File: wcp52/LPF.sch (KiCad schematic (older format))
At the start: 13 parts

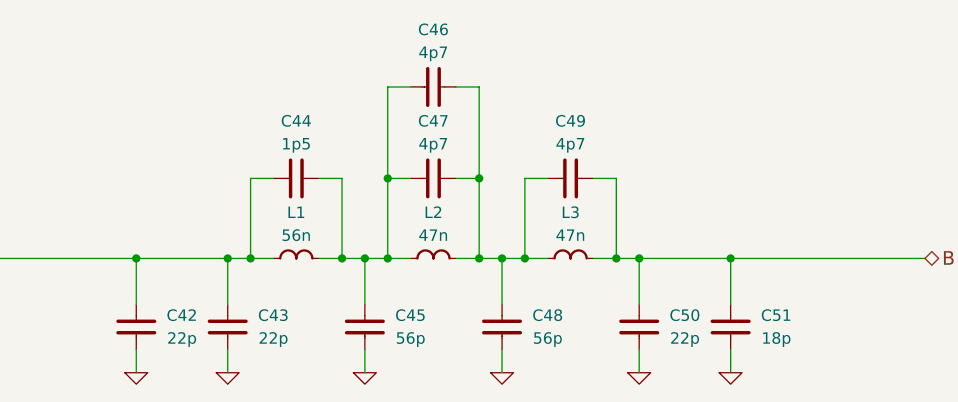
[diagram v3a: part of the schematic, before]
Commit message: Reannotate parts. May need to tweak silkscreen
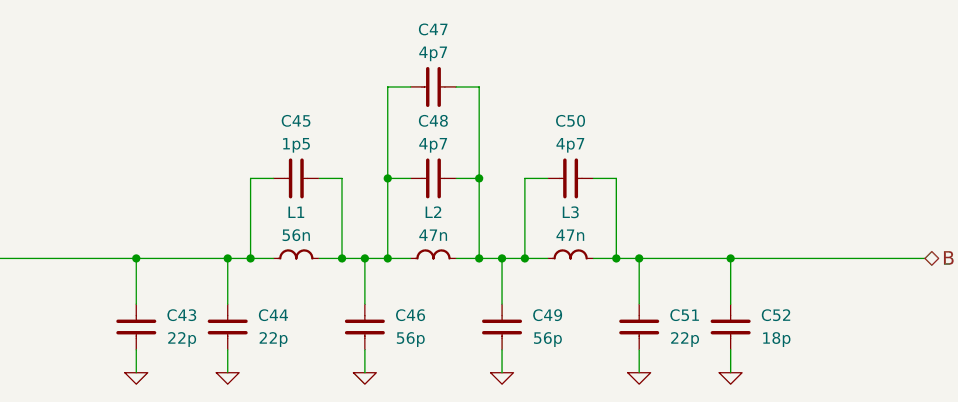
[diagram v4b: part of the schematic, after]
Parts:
- C43: renamed from C42; OldReference (none) -> C42
- C44: renamed from C43; OldReference (none) -> C43
- C45: renamed from C44; OldReference (none) -> C44
- C46: renamed from C45; OldReference (none) -> C45
- C47: renamed from C46; OldReference (none) -> C46
- C48: renamed from C47; OldReference (none) -> C47
- C49: renamed from C48; OldReference (none) -> C48
- C50: renamed from C49; OldReference (none) -> C49
- C51: renamed from C50; OldReference (none) -> C50
- C52: renamed from C51; OldReference (none) -> C51
- L1: OldReference (none) -> L1
- L2: OldReference (none) -> L2
- L3: OldReference (none) -> L3
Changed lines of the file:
@@
 B
 $Comp
-L C-0402 C42
+L C-0402 C43
 U 1 1 54F2BD52
 P 5550 3700
-F 0 "C42" H 5750 3750 50  0000 C CNN
+F 0 "C43" H 5750 3750 50  0000 C CNN
 F 1 "22p" H 5750 3650 50  0000 C CNN
 F 2 "IPC7351-Nominal:CAPC1005X55" H 5550 3700 50  0001 C CNN
@@
 F 5 "Murata" H 5550 3700 60  0001 C CNN "Manuf"
 F 6 "DIST DIGIKEY 490-6219-1-ND" H 6350 4250 60  0001 C CNN "BOM"
+F 7 "C42" H 5550 3700 50  0001 C CNN "OldReference"
 	1    5550 3700
 	1    0    0    -1
@@
 F 5 "Samsung" H 6250 3400 60  0001 C CNN "Manuf"
 F 6 "DIST DIGIKEY 1276-6281-1-ND" H 6250 3400 60  0001 C CNN "BOM"
+F 7 "L1" H 6250 3400 50  0001 C CNN "OldReference"
 	1    6250 3400
 	0    1    1    0
 $EndComp
 $Comp
-L C-0402 C43
+L C-0402 C44
 U 1 1 54F2C0F9
 P 5950 3700
-F 0 "C43" H 6150 3750 50  0000 C CNN
+F 0 "C44" H 6150 3750 50  0000 C CNN
 F 1 "22p" H 6150 3650 50  0000 C CNN
 F 2 "IPC7351-Nominal:CAPC1005X55" H 5950 3700 50  0001 C CNN
@@
 F 5 "Murata" H 5950 3700 60  0001 C CNN "Manuf"
 F 6 "DIST DIGIKEY 490-6219-1-ND" H 6750 4250 60  0001 C CNN "BOM"
+F 7 "C43" H 5950 3700 50  0001 C CNN "OldReference"
 	1    5950 3700
 	1    0    0    -1
 $EndComp
 $Comp
-L C-0402 C44
+L C-0402 C45
 U 1 1 54F2C23D
 P 6250 3050
-F 0 "C44" V 6000 3050 50  0000 C CNN
+F 0 "C45" V 6000 3050 50  0000 C CNN
 F 1 "1p5" V 6100 3050 50  0000 C CNN
 F 2 "IPC7351-Nominal:CAPC1005X55" H 6250 3050 50  0001 C CNN
@@
 F 5 "Samsung" H 6250 3050 60  0001 C CNN "Manuf"
 F 6 "DIST DIGIKEY 1276-1071-1-ND" H 7050 3600 60  0001 C CNN "BOM"
+F 7 "C44" H 6250 3050 50  0001 C CNN "OldReference"
 	1    6250 3050
 	0    1    1    0
@@
 F 5 "Samsung" H 6850 3400 60  0001 C CNN "Manuf"
 F 6 "DIST DIGIKEY 1276-6280-1-ND" H 6850 3400 60  0001 C CNN "BOM"
+F 7 "L2" H 6850 3400 50  0001 C CNN "OldReference"
 	1    6850 3400
 	0    1    1    0
 $EndComp
 $Comp
-L C-0402 C47
+L C-0402 C48
 U 1 1 54F2CACC
 P 6850 3050
-F 0 "C47" V 6600 3050 50  0000 C CNN
+F 0 "C48" V 6600 3050 50  0000 C CNN
 F 1 "4p7" V 6700 3050 50  0000 C CNN
 F 2 "IPC7351-Nominal:CAPC1005X55" H 6850 3050 50  0001 C CNN
@@
 F 5 "Samsung" H 6850 3050 60  0001 C CNN "Manuf"
 F 6 "DIST DIGIKEY 1276-1703-1-ND" H 7650 3600 60  0001 C CNN "BOM"
+F 7 "C47" H 6850 3050 50  0001 C CNN "OldReference"
 	1    6850 3050
 	0    1    1    0
 $EndComp
 $Comp
-L C-0402 C46
+L C-0402 C47
 U 1 1 54F2CB7C
 P 6850 2650
-F 0 "C46" V 6600 2650 50  0000 C CNN
+F 0 "C47" V 6600 2650 50  0000 C CNN
 F 1 "4p7" V 6700 2650 50  0000 C CNN
 F 2 "IPC7351-Nominal:CAPC1005X55" H 6850 2650 50  0001 C CNN
@@
 F 5 "Samsung" H 6850 2650 60  0001 C CNN "Manuf"
 F 6 "DIST DIGIKEY 1276-1703-1-ND" H 7650 3200 60  0001 C CNN "BOM"
+F 7 "C46" H 6850 2650 50  0001 C CNN "OldReference"
 	1    6850 2650
 	0    1    1    0
@@
 F 5 "Samsung" H 7450 3400 60  0001 C CNN "Manuf"
 F 6 "DIST DIGIKEY 1276-6280-1-ND" H 7450 3400 60  0001 C CNN "BOM"
+F 7 "L3" H 7450 3400 50  0001 C CNN "OldReference"
 	1    7450 3400
 	0    1    1    0
 $EndComp
 $Comp
-L C-0402 C49
+L C-0402 C50
 U 1 1 54F2CBED
 P 7450 3050
-F 0 "C49" V 7200 3050 50  0000 C CNN
+F 0 "C50" V 7200 3050 50  0000 C CNN
 F 1 "4p7" V 7300 3050 50  0000 C CNN
 F 2 "IPC7351-Nominal:CAPC1005X55" H 7450 3050 50  0001 C CNN
@@
 F 5 "Samsung" H 7450 3050 60  0001 C CNN "Manuf"
 F 6 "DIST DIGIKEY 1276-1703-1-ND" H 8250 3600 60  0001 C CNN "BOM"
+F 7 "C49" H 7450 3050 50  0001 C CNN "OldReference"
 	1    7450 3050
 	0    1    1    0
 $EndComp
 $Comp
-L C-0402 C45
+L C-0402 C46
 U 1 1 54F2CE50
 P 6550 3700
-F 0 "C45" H 6750 3750 50  0000 C CNN
+F 0 "C46" H 6750 3750 50  0000 C CNN
 F 1 "56p" H 6750 3650 50  0000 C CNN
 F 2 "IPC7351-Nominal:CAPC1005X55" H 6550 3700 50  0001 C CNN
@@
 F 5 "Samsung" H 6550 3700 60  0001 C CNN "Manuf"
 F 6 "DIST DIGIKEY 1276-1707-1-ND" H 7350 4250 60  0001 C CNN "BOM"
+F 7 "C45" H 6550 3700 50  0001 C CNN "OldReference"
 	1    6550 3700
 	1    0    0    -1
 $EndComp
 $Comp
-L C-0402 C48
+L C-0402 C49
 U 1 1 54F2D3A4
 P 7150 3700
-F 0 "C48" H 7350 3750 50  0000 C CNN
+F 0 "C49" H 7350 3750 50  0000 C CNN
 F 1 "56p" H 7350 3650 50  0000 C CNN
 F 2 "IPC7351-Nominal:CAPC1005X55" H 7150 3700 50  0001 C CNN
@@
 F 5 "Samsung" H 7150 3700 60  0001 C CNN "Manuf"
 F 6 "DIST DIGIKEY 1276-1707-1-ND" H 7950 4250 60  0001 C CNN "BOM"
+F 7 "C48" H 7150 3700 50  0001 C CNN "OldReference"
 	1    7150 3700
 	1    0    0    -1
 $EndComp
 $Comp
-L C-0402 C50
+L C-0402 C51
 U 1 1 54F2D3DD
 P 7750 3700
-F 0 "C50" H 7950 3750 50  0000 C CNN
+F 0 "C51" H 7950 3750 50  0000 C CNN
 F 1 "22p" H 7950 3650 50  0000 C CNN
 F 2 "IPC7351-Nominal:CAPC1005X55" H 7750 3700 50  0001 C CNN
@@
 F 5 "Murata" H 7750 3700 60  0001 C CNN "Manuf"
 F 6 "DIST DIGIKEY 490-6219-1-ND" H 8550 4250 60  0001 C CNN "BOM"
+F 7 "C50" H 7750 3700 50  0001 C CNN "OldReference"
 	1    7750 3700
 	1    0    0    -1
 $EndComp
 $Comp
-L C-0402 C51
+L C-0402 C52
 U 1 1 54F2D417
 P 8150 3700
-F 0 "C51" H 8350 3750 50  0000 C CNN
+F 0 "C52" H 8350 3750 50  0000 C CNN
 F 1 "18p" H 8350 3650 50  0000 C CNN
 F 2 "IPC7351-Nominal:CAPC1005X55" H 8150 3700 50  0001 C CNN
@@
 F 5 "Samsung" H 8150 3700 60  0001 C CNN "Manuf"
 F 6 "DIST DIGIKEY 1276-1140-1-ND" H 8950 4250 60  0001 C CNN "BOM"
+F 7 "C51" H 8150 3700 50  0001 C CNN "OldReference"
 	1    8150 3700
 	1    0    0    -1
@@
 F 2 "" H 5550 3900 60  0000 C CNN
 F 3 "" H 5550 3900 60  0000 C CNN
+F 4 "#PWR0157" H 5550 3900 50  0001 C CNN "OldReference"
 	1    5550 3900
 	1    0    0    -1
@@
 F 2 "" H 5950 3900 60  0000 C CNN
 F 3 "" H 5950 3900 60  0000 C CNN
+F 4 "#PWR0158" H 5950 3900 50  0001 C CNN "OldReference"
 	1    5950 3900
 	1    0    0    -1
@@
 F 2 "" H 6550 3900 60  0000 C CNN
 F 3 "" H 6550 3900 60  0000 C CNN
+F 4 "#PWR0159" H 6550 3900 50  0001 C CNN "OldReference"
 	1    6550 3900
 	1    0    0    -1
@@
 F 2 "" H 7150 3900 60  0000 C CNN
 F 3 "" H 7150 3900 60  0000 C CNN
+F 4 "#PWR0160" H 7150 3900 50  0001 C CNN "OldReference"
 	1    7150 3900
 	1    0    0    -1
@@
 F 2 "" H 7750 3900 60  0000 C CNN
 F 3 "" H 7750 3900 60  0000 C CNN
+F 4 "#PWR0161" H 7750 3900 50  0001 C CNN "OldReference"
 	1    7750 3900
 	1    0    0    -1
@@
 F 2 "" H 8150 3900 60  0000 C CNN
 F 3 "" H 8150 3900 60  0000 C CNN
+F 4 "#PWR0162" H 8150 3900 50  0001 C CNN "OldReference"
 	1    8150 3900
 	1    0    0    -1

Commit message: Schematic touchups
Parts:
- C45: BOM DIST DIGIKEY 1276-1071-1-ND -> DIST DIGIKEY 1276-1656-1-ND
- C52: value 18p -> 22p; BOM DIST DIGIKEY 1276-1140-1-ND -> DIST DIGIKEY 490-6219-1-ND; Manuf Samsung -> Murata; PN CL05C180JB5NNNC -> GRM1555C1H220GA01D
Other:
- note added: "Intended frequency response of filter:"

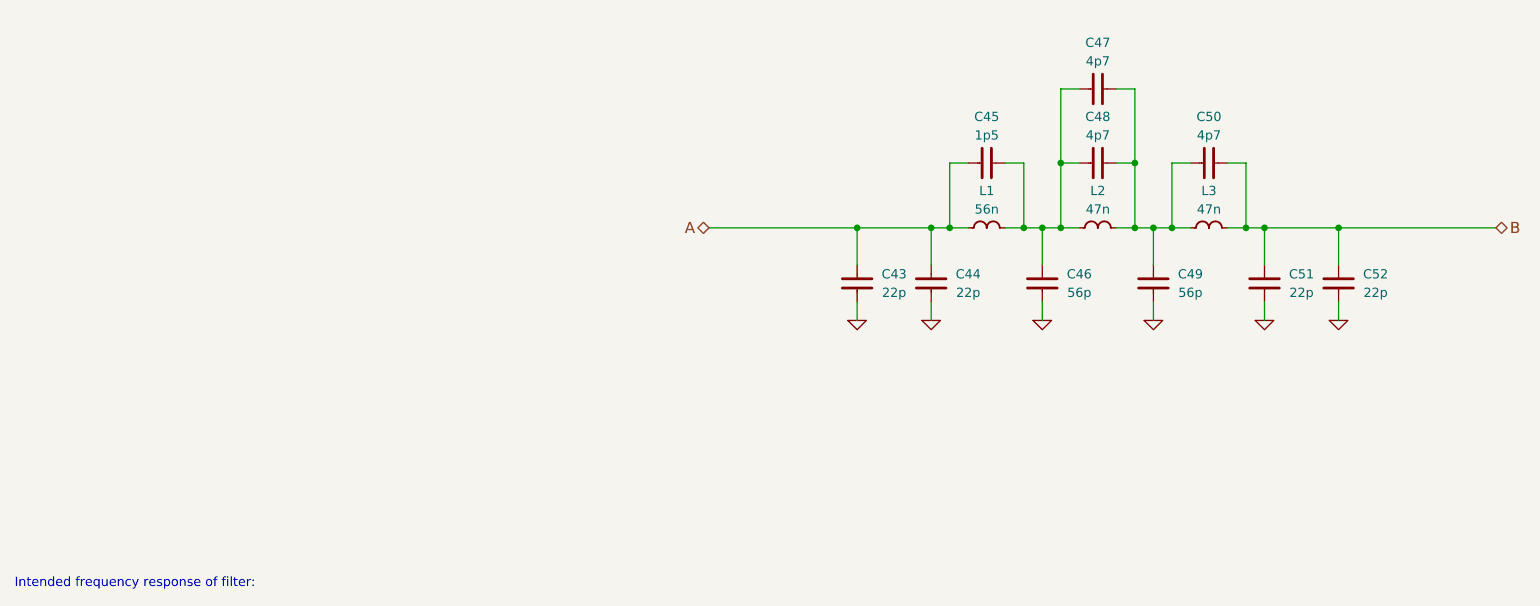
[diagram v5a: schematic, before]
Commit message: Change schematic pages to letter size
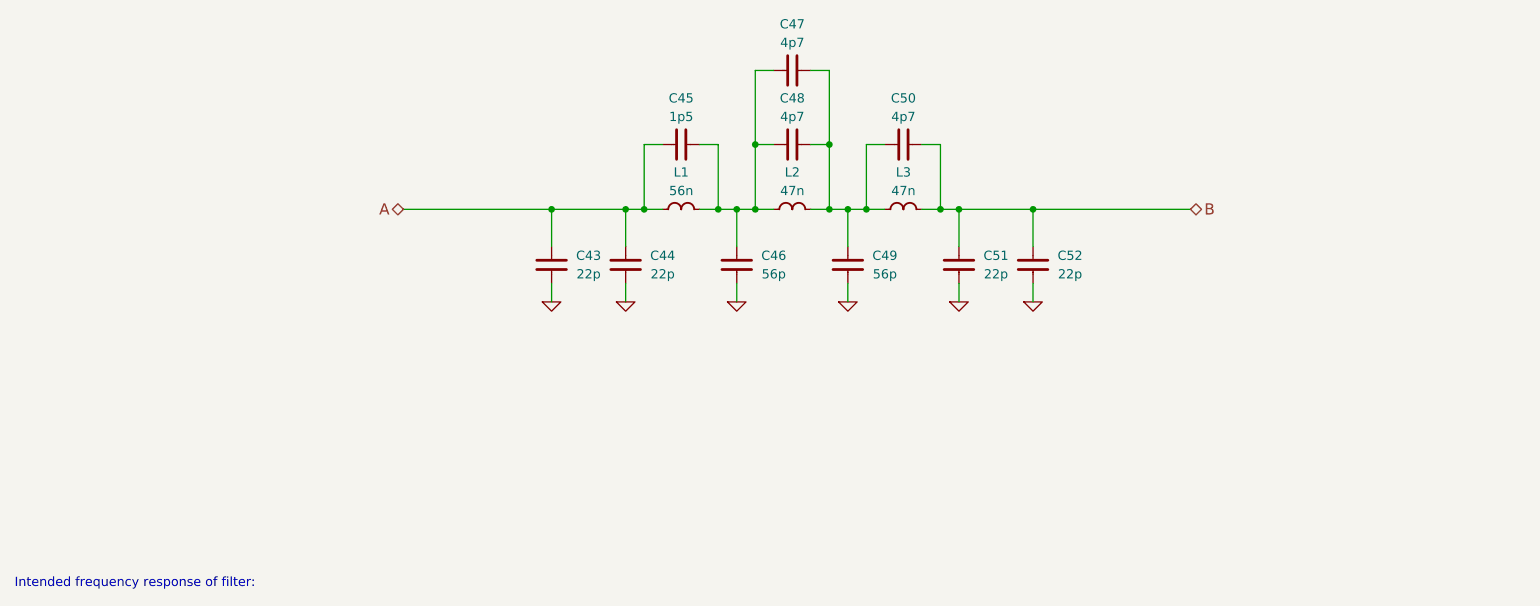
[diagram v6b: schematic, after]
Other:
- moved on the sheet: C43, C44, C45, C46, C47, C48, C49, C50, C51, C52, L1, L2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
